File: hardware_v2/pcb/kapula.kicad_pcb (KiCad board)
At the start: 4 copper layers, 50 x 59 mm, 166 parts, among them J1 Conn_02x10_Odd_Even, J2 Conn_02x10_Odd_Even, J3 U.FL, J4 U.FL, J5 U.FL, J6 U.FL, Q1 AO3401A, Q2 AO3400A, Q3 AO3400A, Q4 AO3400A, Q5 AO3401A, Q6 BSS84, T1 BW21S7511A01TF, T2 BW21S7511A01TF, T3 BW21S7511A01TF, T4 BW21S7511A01TF, U1 TP4054, U2 DW01+G, U3 XC6206P332MR, U4 FM8002A, U5 EFR32FG14P233F256GM48-B, U6 TG2016SMN 38.4000M-MCGNNM3, U7 XA213-G4J, Y1 32768 Hz

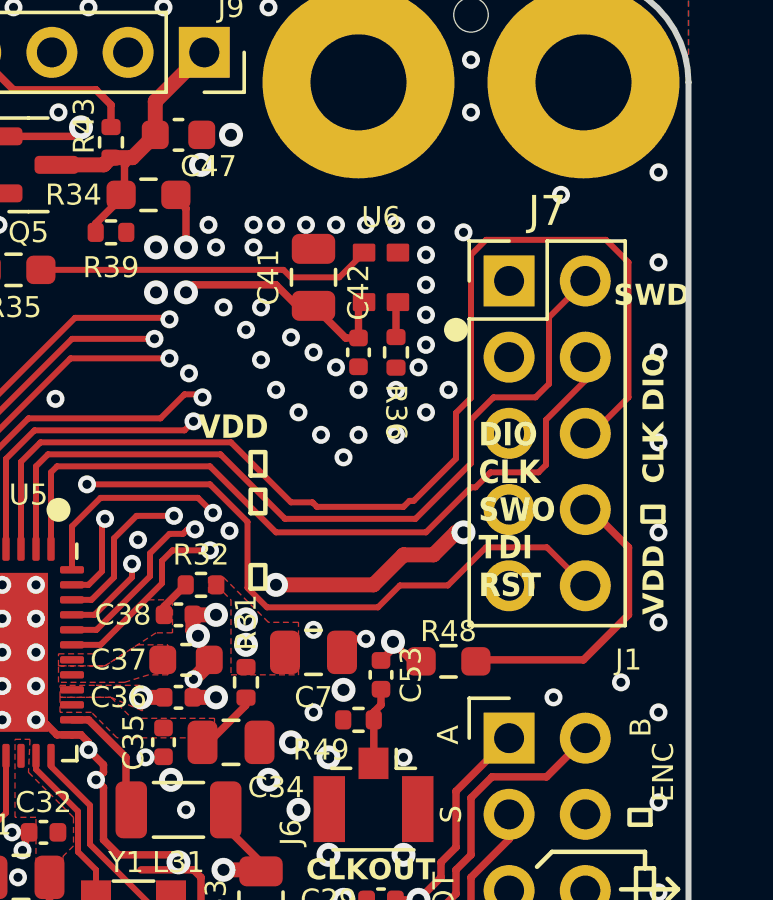
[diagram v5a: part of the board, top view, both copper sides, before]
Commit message: PCB: Fix some silkscreen texts
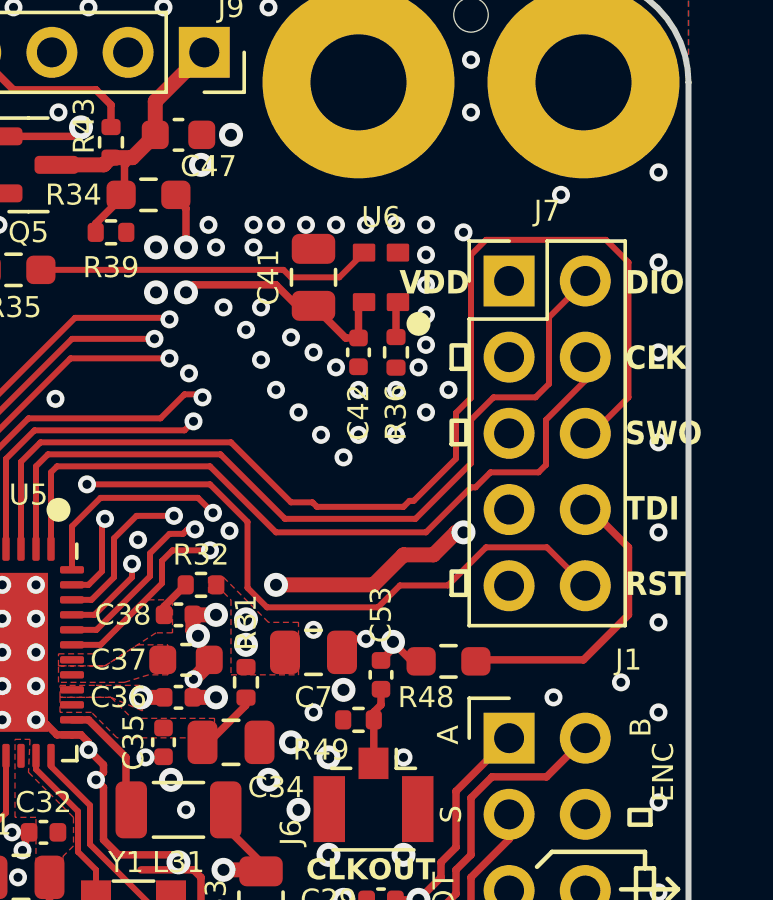
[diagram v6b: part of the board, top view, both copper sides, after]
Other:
- board text removed: "SWD"
- board text removed: "SWDIO SWCLK GND VDD"
- board text removed: "VDD ⏚ CLK DIO"
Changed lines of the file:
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@@
     (property "ki_keywords" "cap capacitor")
     (attr smd)
-    (fp_text reference "C42" (at -2 0 90 unlocked) (layer "F.SilkS")
+    (fp_text reference "C42" (at 2 0 90 unlocked) (layer "F.SilkS")
         (effects (font (size 0.7 0.7) (thickness 0.15)))
     )
@@
     (property "ki_keywords" "R res resistor")
     (attr smd)
-    (fp_text reference "R36" (at 2 0 -90 unlocked) (layer "F.SilkS")
+    (fp_text reference "R36" (at 2 0 90 unlocked) (layer "F.SilkS")
         (effects (font (size 0.7 0.7) (thickness 0.15)))
     )
@@
     (property "ki_keywords" "R res resistor")
     (attr smd)
-    (fp_text reference "R48" (at 0 -1 unlocked) (layer "F.SilkS")
+    (fp_text reference "R48" (at -0.75 1.2 unlocked) (layer "F.SilkS")
         (effects (font (size 0.7 0.7) (thickness 0.15)))
     )
@@
     (property "ki_keywords" "Cortex Debug Connector ARM SWD JTAG")
     (attr through_hole)
-    (fp_text reference "J7" (at 1.27 -2.33) (layer "F.SilkS")
-        (effects (font (size 1 1) (thickness 0.15)))
+    (fp_text reference "J7" (at 1.27 -2.33 unlocked) (layer "F.SilkS")
+        (effects (font (size 0.7 0.7) (thickness 0.15)))
     )
     (fp_text value "~" (at 1.27 12.49) (layer "F.Fab")
@@
     (property "ki_keywords" "cap capacitor")
     (attr smd)
-    (fp_text reference "C53" (at 0 -1 -270 unlocked) (layer "F.SilkS")
+    (fp_text reference "C53" (at -2 0 -270 unlocked) (layer "F.SilkS")
         (effects (font (size 0.7 0.7) (thickness 0.15)))
     )
@@
   (gr_circle (center 123.25 106.9) (end 123.45 106.9)
     (stroke (width 0.4) (type solid)) (fill none) (layer "F.SilkS"))
-  (gr_circle (center 142.25 69.25) (end 142.45 69.25)
+  (gr_circle (center 141 69.05) (end 141.2 69.05)
     (stroke (width 0.4) (type solid)) (fill none) (layer "F.SilkS"))
   (gr_line (start 146.5 116.5) (end 103.5 116.5)
@@
     (effects (font (size 0.7 0.7) (thickness 0.15) bold) (justify bottom mirror))
   )
+  (gr_text "VDD\n\n⏚\n\n⏚\n\n\n\n⏚" (at 142.7 72.7) (layer "B.SilkS")
+    (effects (font (size 0.78 0.7) (thickness 0.15) bold) (justify left mirror))
+  )
   (gr_text "BAT-" (at 149 103.5 90) (layer "B.SilkS")
     (effects (font (size 0.7 0.7) (thickness 0.15)) (justify bottom mirror))
@@
     (effects (font (size 0.7 0.7) (thickness 0.15)) (justify bottom mirror))
   )
+  (gr_text "DIO\n\nCLK\n\nSWO\n\nTDI\n\nRST" (at 147.89 72.7) (layer "B.SilkS")
+    (effects (font (size 0.78 0.7) (thickness 0.15) bold) (justify right mirror))
+  )
   (gr_text "⏚" (at 100.75 93 -90) (layer "B.SilkS")
     (effects (font (size 0.7 0.7) (thickness 0.15)) (justify bottom mirror))
@@
     (effects (font (size 0.7 0.7) (thickness 0.15) bold) (justify bottom mirror))
   )
-  (gr_text "SWDIO\n\nSWCLK\n\nGND\n\nVDD" (at 144.5 74) (layer "B.SilkS")
-    (effects (font (size 0.8 0.8) (thickness 0.15) bold) (justify left mirror))
-  )
   (gr_text "⏚" (at 100.75 82.75 -90) (layer "B.SilkS")
     (effects (font (size 0.7 0.7) (thickness 0.15)) (justify bottom mirror))
@@
     (effects (font (size 0.7 0.7) (thickness 0.15)) (justify right bottom mirror))
   )
-  (gr_text "SWD" (at 147.5 68.5) (layer "F.SilkS")
-    (effects (font (size 0.7 0.7) (thickness 0.15) bold) (justify left bottom))
-  )
   (gr_text "PTT" (at 142.25 95.5 90) (layer "F.SilkS")
     (effects (font (size 0.7 0.7) (thickness 0.15)) (justify bottom))
@@
     (effects (font (size 0.7 0.7) (thickness 0.15)) (justify bottom))
   )
-  (gr_text "VDD  ⏚  CLK DIO" (at 149.25 78.75 90) (layer "F.SilkS")
-    (effects (font (size 0.7 0.7) (thickness 0.15) bold) (justify left bottom))
-  )
   (gr_text "TX\nEN" (at 107.75 83 -90) (layer "F.SilkS")
     (effects (font (size 0.7 0.7) (thickness 0.15) bold) (justify bottom))
@@
     (effects (font (size 0.7 0.7) (thickness 0.15) bold) (justify bottom))
   )
-  (gr_text "VDD\n⏚\n⏚\n\n⏚" (at 136 75) (layer "F.SilkS")
+  (gr_text "VDD\n\n⏚\n\n⏚\n\n\n\n⏚" (at 142.7 72.7) (layer "F.SilkS")
     (effects (font (size 0.78 0.7) (thickness 0.15) bold) (justify right))
   )
@@
     (effects (font (size 0.7 0.7) (thickness 0.15)) (justify bottom))
   )
-  (gr_text "DIO\nCLK\nSWO\nTDI\nRST" (at 143 75.25) (layer "F.SilkS")
+  (gr_text "DIO\n\nCLK\n\nSWO\n\nTDI\n\nRST" (at 147.89 72.7) (layer "F.SilkS")
     (effects (font (size 0.78 0.7) (thickness 0.15) bold) (justify left))
   )
